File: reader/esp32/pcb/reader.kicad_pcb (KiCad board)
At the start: 2 copper layers, 68.2 x 31.9 mm, 25 parts, among them J1 Debug, J2 RS485, Q1 MMBT3904, Q2 MMBT3904, U1 ESP32-WROOM-32U, U2 RDM6300, U3 MAX485E, U5 AMS1117-3.3

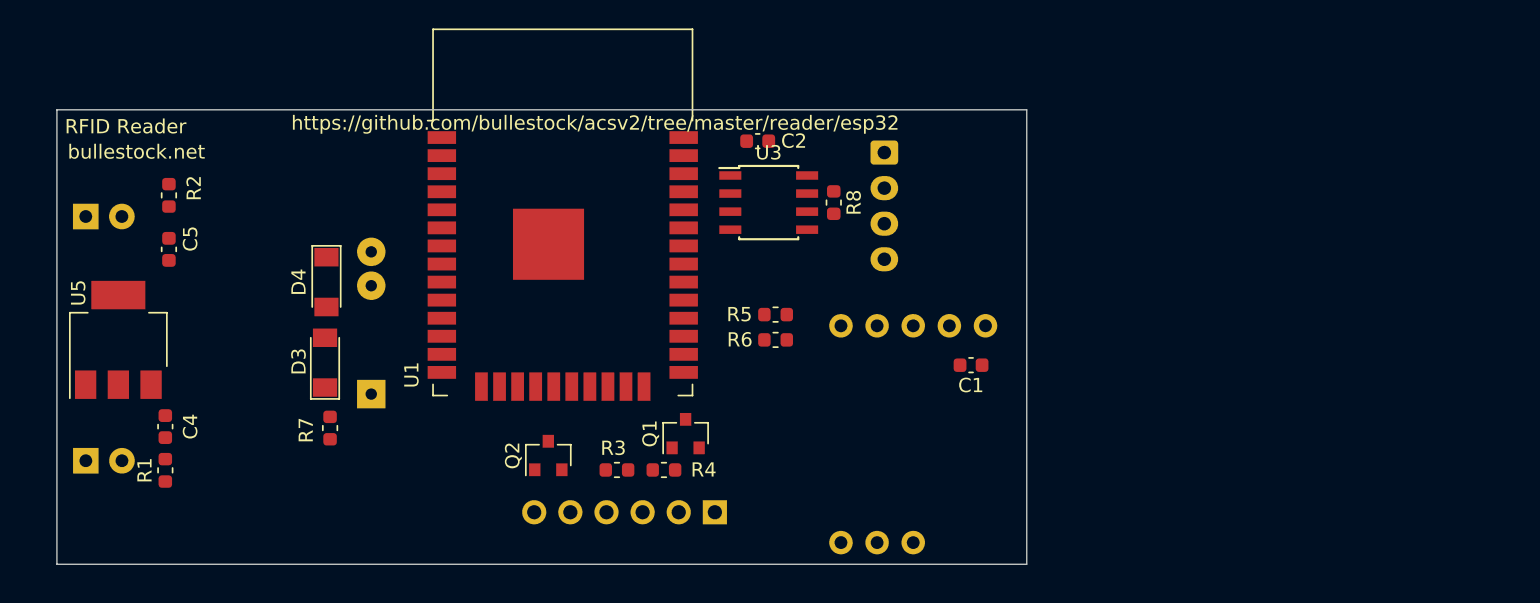
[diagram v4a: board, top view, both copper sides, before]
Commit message: Change to WROOM32U.
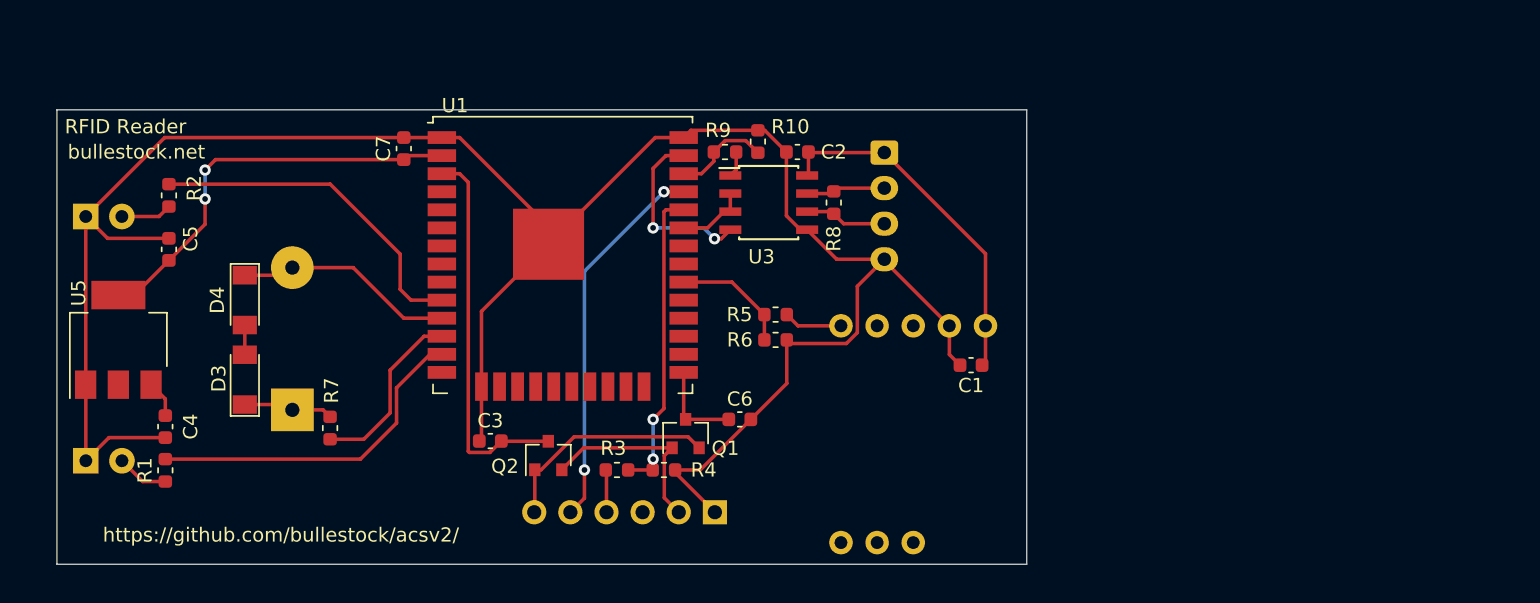
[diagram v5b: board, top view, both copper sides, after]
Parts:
- added C3: 100n, Capacitor_SMD:C_0603_1608Metric, F.Cu at (74.9, 65.8)
- added C6: 100n, Capacitor_SMD:C_0603_1608Metric, F.Cu at (92.5, 64.3)
- added C7: 100n, Capacitor_SMD:C_0603_1608Metric, F.Cu at (68.8, 45.2)
- added R10: 2k2, Resistor_SMD:R_0603_1608Metric, F.Cu at (93.7, 44.7)
- added R9: 1k2, Resistor_SMD:R_0603_1608Metric, F.Cu at (91.4, 45.5)
- BZ1: value Murata PKM22EPP-40S1-B0 -> Buzzer; footprint Module:Buzzer_D14mm_H7mm_P7.62mm -> Module:Buzzer_D22mm_H8mm_P10mm
- U1: footprint RF_Module:ESP32-WROOM-32 -> RF_Module:ESP32-WROOM-32U
- moved BZ1 6.78 mm to (61.0, 58.6)
- moved D4 5.88 mm to (57.7, 55.9)
- moved D3 5.76 mm to (57.7, 61.5)
- moved C2 2.90 mm to (96.5, 45.5)
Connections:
- U1 pad 33: RTS -> RTS485
- U3 pad 1: RX485 -> Net-(U3-RO)
- U3 pad 2: RTS -> RTS485
- U3 pad 3: RTS -> RTS485
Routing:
- net GND: track 0.00 -> 156.3 mm
- net +3V3: track 0.00 -> 29.0 mm, vias 0 -> 2
- net +5V: track 0.00 -> 27.6 mm
- net RESET: track 0.00 -> 27.0 mm
- net ESP_TX: track 0.00 -> 26.6 mm, vias 0 -> 2
- net GREEN: track 0.00 -> 24.0 mm
- net RED: track 0.00 -> 23.9 mm
- net ESP_RX: track 0.00 -> 21.6 mm, vias 0 -> 2
- net DTR: track 0.00 -> 15.8 mm
- net BUZ2: track 0.00 -> 15.5 mm
- net RTS: track 0.00 -> 13.6 mm
- net TX485: track 0.00 -> 12.7 mm, vias 0 -> 2
- net BUZ1: track 0.00 -> 12.6 mm
- net ESP_RFID_TX: track 0.00 -> 8.40 mm
- net RX485: track 0.00 -> 7.10 mm
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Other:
- board text added: "https://github.com/bullestock/acsv2/"
- board text removed: "https://github.com/bullestock/acsv2/tree/master/reader/esp32"

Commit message: Complete routing.
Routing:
- net +5V: track 27.6 -> 105.1 mm, vias 0 -> 2
- net GND: track 156.3 -> 170.1 mm
- net +3V3: track 29.0 -> 35.3 mm
- added copper zone on B.Cu, net GND
- added copper zone on F.Cu, net GND

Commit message: Final adjustments, order.
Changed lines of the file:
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@@
   )
   (paper "A4")
+  (title_block
+    (comment 4 "AISLER Project ID: ELMSVNFD")
+  )
   (layers
     (0 "F.Cu" signal)
@@
       (effects (font (size 1 1) (thickness 0.15)) (justify mirror))
     )
-    (pad "1" thru_hole roundrect (at 0 0 270) (size 1.7 1.95) (drill 0.95) (layers "*.Cu" "*.Mask") (roundrect_rratio 0.147059)
+    (pad "1" thru_hole roundrect (at 0 0 270) (size 1.7 1.95) (drill 0.95) (layers "*.Cu" "*.Mask") (roundrect_rratio 0.1470588235)
       (net 3 "+5V") (pinfunction "Pin_1") (pintype "passive"))
     (pad "2" thru_hole oval (at 2.5 0 270) (size 1.7 1.95) (drill 0.95) (layers "*.Cu" "*.Mask")

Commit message: Remove capacitors.
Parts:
- removed C3, C6: 100n, Capacitor_SMD:C_0603_1608Metric
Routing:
- net GND: track 170.1 -> 166.2 mm
- net BOOT: track 6.39 -> 3.36 mm
- net RESET: track 27.0 -> 24.4 mm
